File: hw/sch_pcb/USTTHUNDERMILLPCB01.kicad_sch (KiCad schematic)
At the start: 13 parts, among them J2 SM03B-GHS-TB, U1 ISL21080DIH312Z-TK 1V25, U2 OPA314

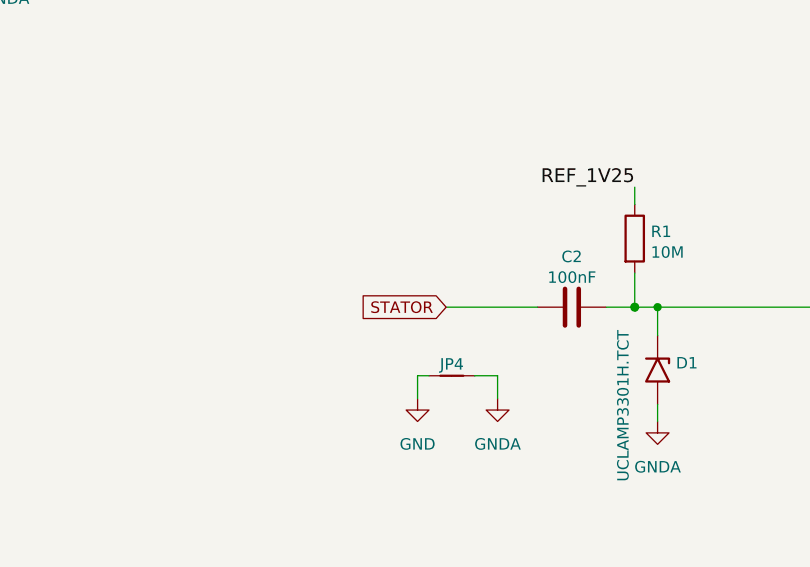
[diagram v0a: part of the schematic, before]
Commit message: pridani testopintu pro pripojeni externi elektrody
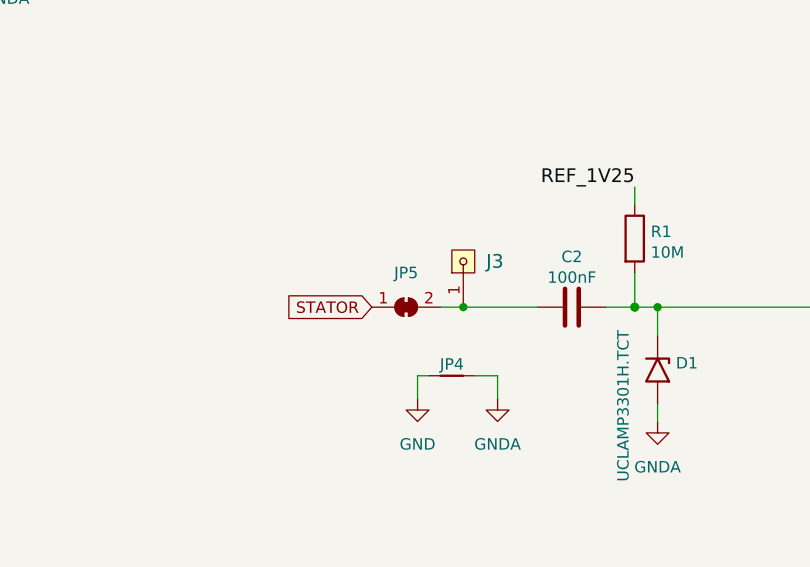
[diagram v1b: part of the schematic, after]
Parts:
- added J3: HEADER_1x01, Mlab_Pin_Headers:Straight_1x01, symbol MLAB_HEADER:HEADER_1x01
- added JP5: SolderJumper_2_Bridged, Jumper:SolderJumper-2_P1.3mm_Bridged_RoundedPad1.0x1.5mm, symbol Jumper:SolderJumper_2_Bridged
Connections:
- net STATOR: now also JP5.1 (A); no longer C2.1
- new net: C2.1, J3.1, JP5.2 (B)
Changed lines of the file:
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@@
   (junction (at 109.22 78.74) (diameter 0) (color 0 0 0 0)
   )
+  (junction (at 87.63 78.74) (diameter 0) (color 0 0 0 0)
+  )
   (junction (at 128.27 100.33) (diameter 1.016) (color 0 0 0 0)
   )
@@
     (stroke (width 0) (type solid))
   )
-  (wire (pts (xy 85.725 78.74) (xy 95.885 78.74))
+  (wire (pts (xy 85.09 78.74) (xy 87.63 78.74))
     (stroke (width 0) (type solid))
   )
@@
   )
   (wire (pts (xy 109.22 89.535) (xy 109.22 91.44))
+    (stroke (width 0) (type solid))
+  )
+  (wire (pts (xy 87.63 78.74) (xy 95.885 78.74))
     (stroke (width 0) (type solid))
   )
@@
     )
   )
-  (global_label "STATOR" (shape input) (at 85.725 78.74 180) (fields_autoplaced)
+  (global_label "STATOR" (shape input) (at 77.47 78.74 180) (fields_autoplaced)
     (effects (font (size 1.27 1.27)) (justify right))
-    (property "Intersheetrefs" "${INTERSHEET_REFS}" (at 76.4781 78.6606 0)
+    (property "Intersheetrefs" "${INTERSHEET_REFS}" (at 68.2231 78.6606 0)
       (effects (font (size 1.27 1.27)) (justify right) hide)
     )
@@
     )
   )
+  (symbol (lib_id "Jumper:SolderJumper_2_Bridged") (at 81.28 78.74 0) (unit 1)
+    (in_bom yes) (on_board yes) (dnp no) (fields_autoplaced)
+    (property "Reference" "JP5" (at 81.28 74.93 0)
+      (effects (font (size 1.27 1.27)))
+    )
+    (property "Value" "SolderJumper_2_Bridged" (at 81.28 74.93 0)
+      (effects (font (size 1.27 1.27)) hide)
+    )
+    (property "Footprint" "Jumper:SolderJumper-2_P1.3mm_Bridged_RoundedPad1.0x1.5mm" (at 81.28 78.74 0)
+      (effects (font (size 1.27 1.27)) hide)
+    )
+    (property "Datasheet" "~" (at 81.28 78.74 0)
+      (effects (font (size 1.27 1.27)) hide)
+    )
+    (pin "1")
+    (pin "2")
+    (instances
+      (project "USTTHUNDERMILLPCB01"
+        (path "/6990ffb7-4abe-4df9-bce7-87822fc68e4c"
+          (reference "JP5") (unit 1)
+        )
+      )
+    )
+  )
   (symbol (lib_id "Device:R") (at 128.27 113.03 180) (unit 1)
     (in_bom yes) (on_board yes) (dnp no)
@@
         )
       )
+    )
+  )
+  (symbol (lib_id "MLAB_HEADER:HEADER_1x01") (at 87.63 73.66 90) (unit 1)
+    (in_bom yes) (on_board yes) (dnp no) (fields_autoplaced)
+    (property "Reference" "J3" (at 90.17 73.66 90)
+      (effects (font (size 1.524 1.524)) (justify right))
+    )
+    (property "Value" "HEADER_1x01" (at 90.17 74.93 90)
+      (effects (font (size 1.524 1.524)) (justify right) hide)
+    )
+    (property "Footprint" "Mlab_Pin_Headers:Straight_1x01" (at 87.63 73.66 0)
+      (effects (font (size 1.524 1.524)) hide)
+    )
+    (property "Datasheet" "" (at 87.63 73.66 0)
+      (effects (font (size 1.524 1.524)))
+    )
+    (pin "1")
+    (instances
+      (project "USTTHUNDERMILLPCB01"
+        (path "/6990ffb7-4abe-4df9-bce7-87822fc68e4c"
+          (reference "J3") (unit 1)
+        )
+      )
